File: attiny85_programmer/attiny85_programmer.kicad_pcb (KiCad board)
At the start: 2 copper layers, 8.2 x 5 mm, 17 parts, among them P1 USB_C_Plug_USB2.0, U2 ATtiny85-20P

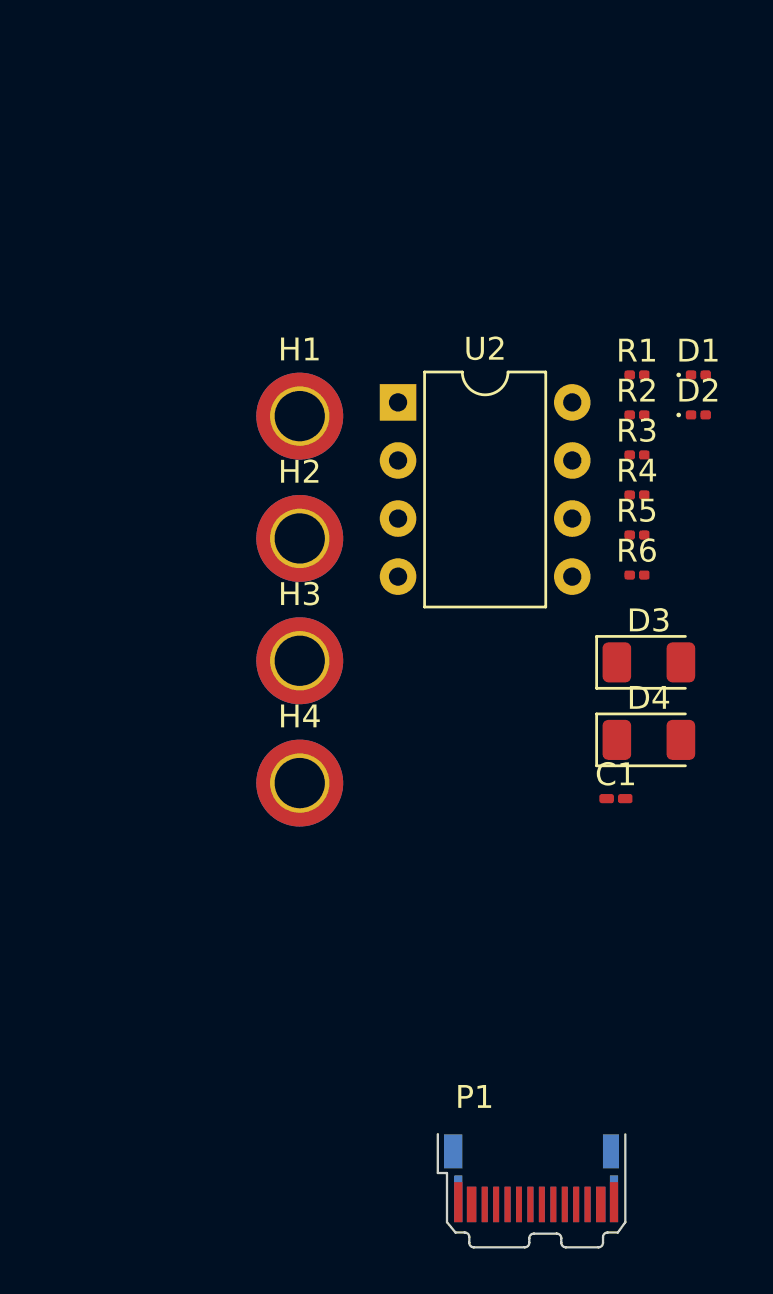
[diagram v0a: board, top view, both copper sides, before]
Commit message: ATtiny85 Programmer
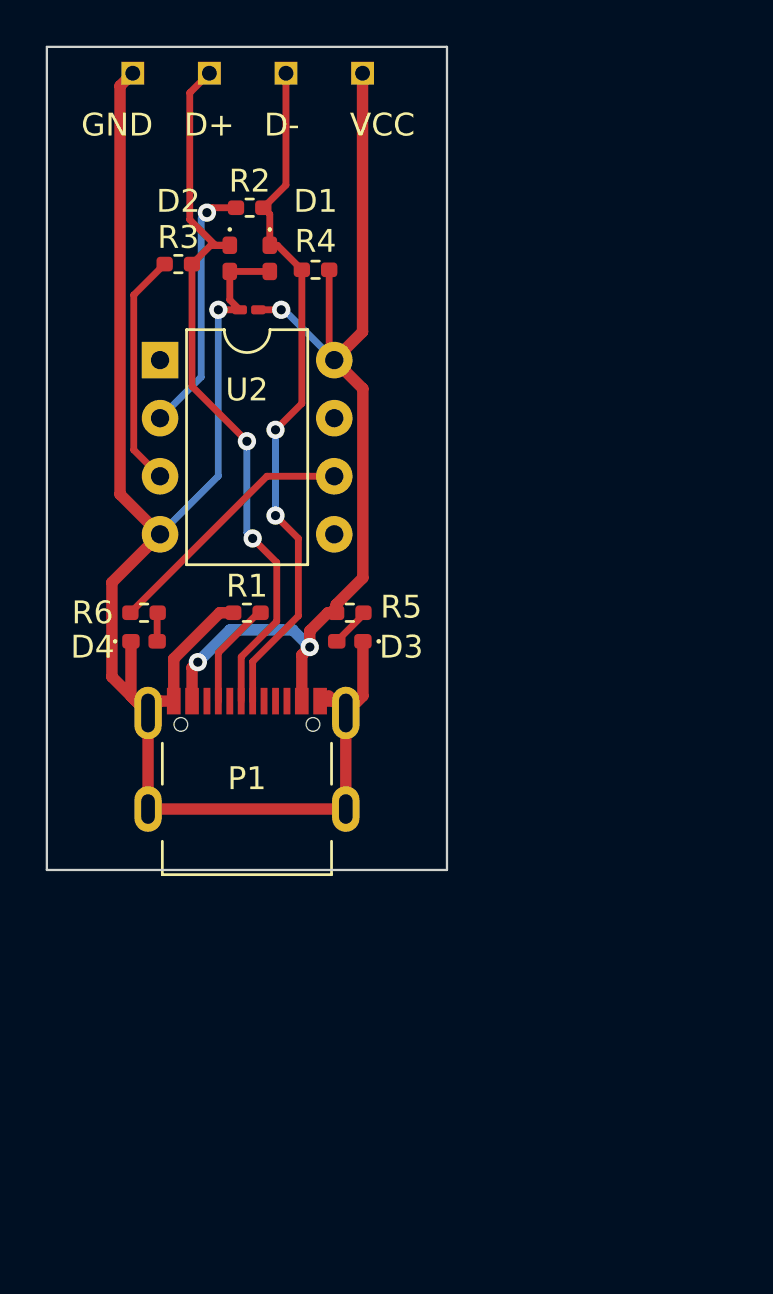
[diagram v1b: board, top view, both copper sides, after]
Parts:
- D1, D2: footprint Diode_SMD:D_0201_0603Metric -> Diode_SMD:D_0402_1005Metric_Pad0.77x0.64mm_HandSolder
- D3, D4: footprint LED_SMD:LED_1206_3216Metric -> LED_SMD:LED_0402_1005Metric_Pad0.77x0.64mm_HandSolder
- H1, H2, H3, H4: footprint MountingHole:MountingHole_2.2mm_M2_DIN965_Pad_TopBottom -> Connector_PinHeader_1.27mm:PinHeader_1x01_P1.27mm_Horizontal; moved to B.Cu
- P1: footprint Connector_USB:USB_C_Plug_JAE_DX07P024AJ1 -> Library:TYPE-C 16PIN 2MD(073)
- R1, R2, R3, R4, R5, R6: footprint Resistor_SMD:R_0201_0603Metric -> Resistor_SMD:R_0402_1005Metric_Pad0.72x0.64mm_HandSolder
- moved H4 31.9 mm to (133.5, 69.9), turned to 90 degrees
- moved C1 26.7 mm to (138.6, 80.2), turned to 180 degrees
- moved H3 26.0 mm to (136.9, 69.9), turned to 90 degrees
- moved D4 22.5 mm to (134.0, 94.8)
- moved P1 22.3 mm to (138.5, 99.9)
- moved R3 21.7 mm to (135.5, 78.2)
- moved R6 21.6 mm to (134.0, 93.5)
- moved D2 21.6 mm to (137.8, 78.0), turned to -90 degrees
- moved H2 20.4 mm to (140.2, 69.9), turned to 90 degrees
- moved R1 20.0 mm to (138.5, 93.5)
- moved D1 19.4 mm to (139.5, 78.0), turned to -90 degrees
- moved R2 19.2 mm to (138.6, 75.8)
- moved R4 17.2 mm to (141.5, 78.5), turned to 180 degrees
- moved H1 15.2 mm to (143.6, 69.9), turned to 90 degrees
- moved D3 13.1 mm to (143.0, 94.8), turned to 180 degrees
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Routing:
- net GND: track 0.00 -> 78.9 mm, vias 0 -> 1
- net VBUS: track 0.00 -> 45.8 mm, vias 0 -> 3
- net /PIN3: track 0.00 -> 32.5 mm, vias 0 -> 2
- net /PIN2: track 0.00 -> 30.5 mm, vias 0 -> 2
- net /PIN6: track 0.00 -> 11.4 mm
- net Net-(U2-XTAL1/PB3): track 0.00 -> 11.2 mm, vias 0 -> 1
- net Net-(U2-XTAL2/PB4): track 0.00 -> 10.3 mm
- net Net-(P1-CC): track 0.00 -> 4.69 mm
- net Net-(D3-A): track 0.00 -> 1.73 mm
- net Net-(D4-A): track 0.00 -> 1.26 mm
- added copper zone on B.Cu, net GND
- added copper zone on F.Cu, net GND
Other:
- board size 8.2 x 5 mm -> 17.5 x 36 mm
- board text added: "D+"
- board text added: "D-"
- board text added: "GND"
- board text added: "VCC"
